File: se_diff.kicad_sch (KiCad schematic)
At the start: 12 parts

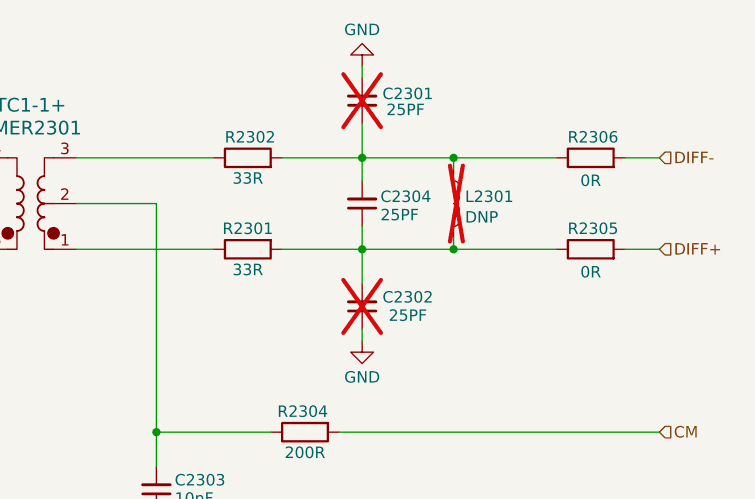
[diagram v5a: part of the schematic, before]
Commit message: Final changes
-Changed ADC input filter caps from 25pF to 5pF
-Added a spot to silkscreen a SN on the back of the board
-Moved some of the silkscreen logo to avoid via overlaps.
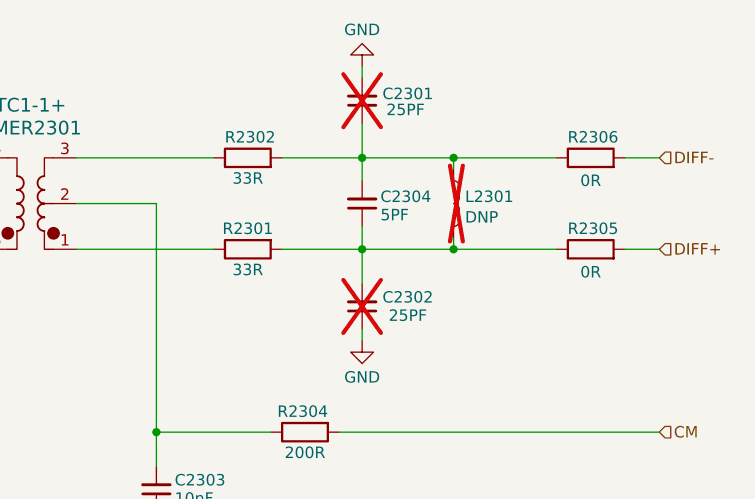
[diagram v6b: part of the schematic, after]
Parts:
- C2304: value 25PF -> 5PF; Manufacturer Samsung -> Kemet; Manufacturer Part Number CL10C250JB8NNNC -> CBR06C509A5GAC; Vendor digikey:1276-2244-1-ND -> digikey:399-17323-1-ND
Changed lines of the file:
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@@
 			)
 		)
-		(property "Value" "25PF"
+		(property "Value" "5PF"
 			(at 126.492 54.6099 0)
 			(effects
@@
 			)
 		)
-		(property "Description" "CAP CER 25PF 50V C0G/NP0 0603"
+		(property "Description" "CAP CER 5PF 50V C0G/NP0 0603"
 			(at 124.46 53.34 0)
 			(effects
@@
 			)
 		)
-		(property "Vendor" "digikey:1276-2244-1-ND"
+		(property "Vendor" "digikey:399-17323-1-ND"
 			(at -82.55 -25.4 0)
 			(effects
@@
 			)
 		)
-		(property "Manufacturer" "Samsung"
+		(property "Manufacturer" "Kemet"
 			(at 124.46 53.34 0)
 			(effects
@@
 			)
 		)
-		(property "Manufacturer Part Number" "CL10C250JB8NNNC "
+		(property "Manufacturer Part Number" "CBR06C509A5GAC"
 			(at 124.46 53.34 0)
 			(effects
